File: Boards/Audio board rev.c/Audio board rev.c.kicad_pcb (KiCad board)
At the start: 2 copper layers, 165.9 x 187.4 mm, 110 parts, among them J1 CEC card edge connector large, U1 6821, U10 LM324, U11 MC1458, U2 LM339, U3 LM339, U4 ULN2003A, U5 DAC-08, U6 DAC-08, U7 DAC-08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

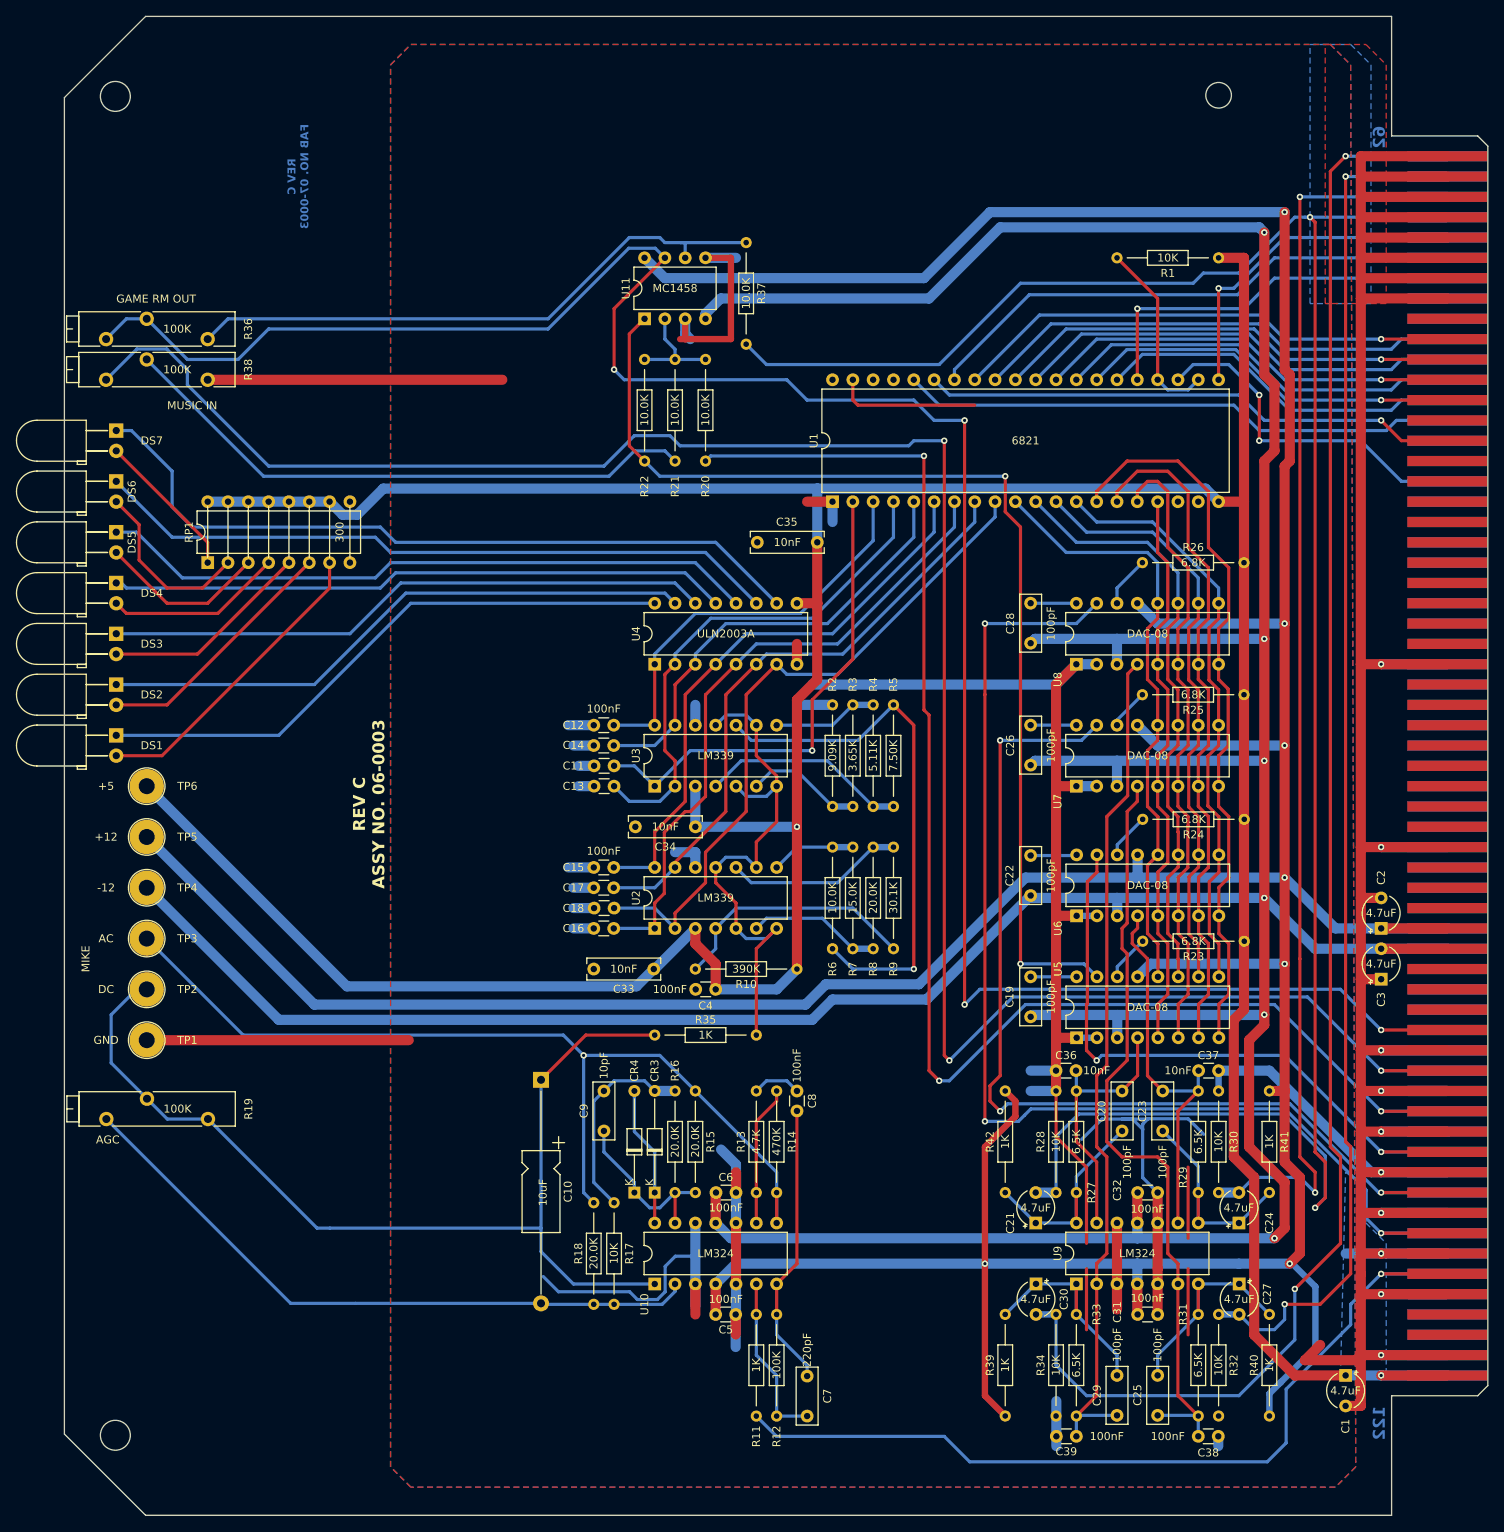
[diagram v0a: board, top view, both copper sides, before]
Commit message: tweaked copper fills on revc
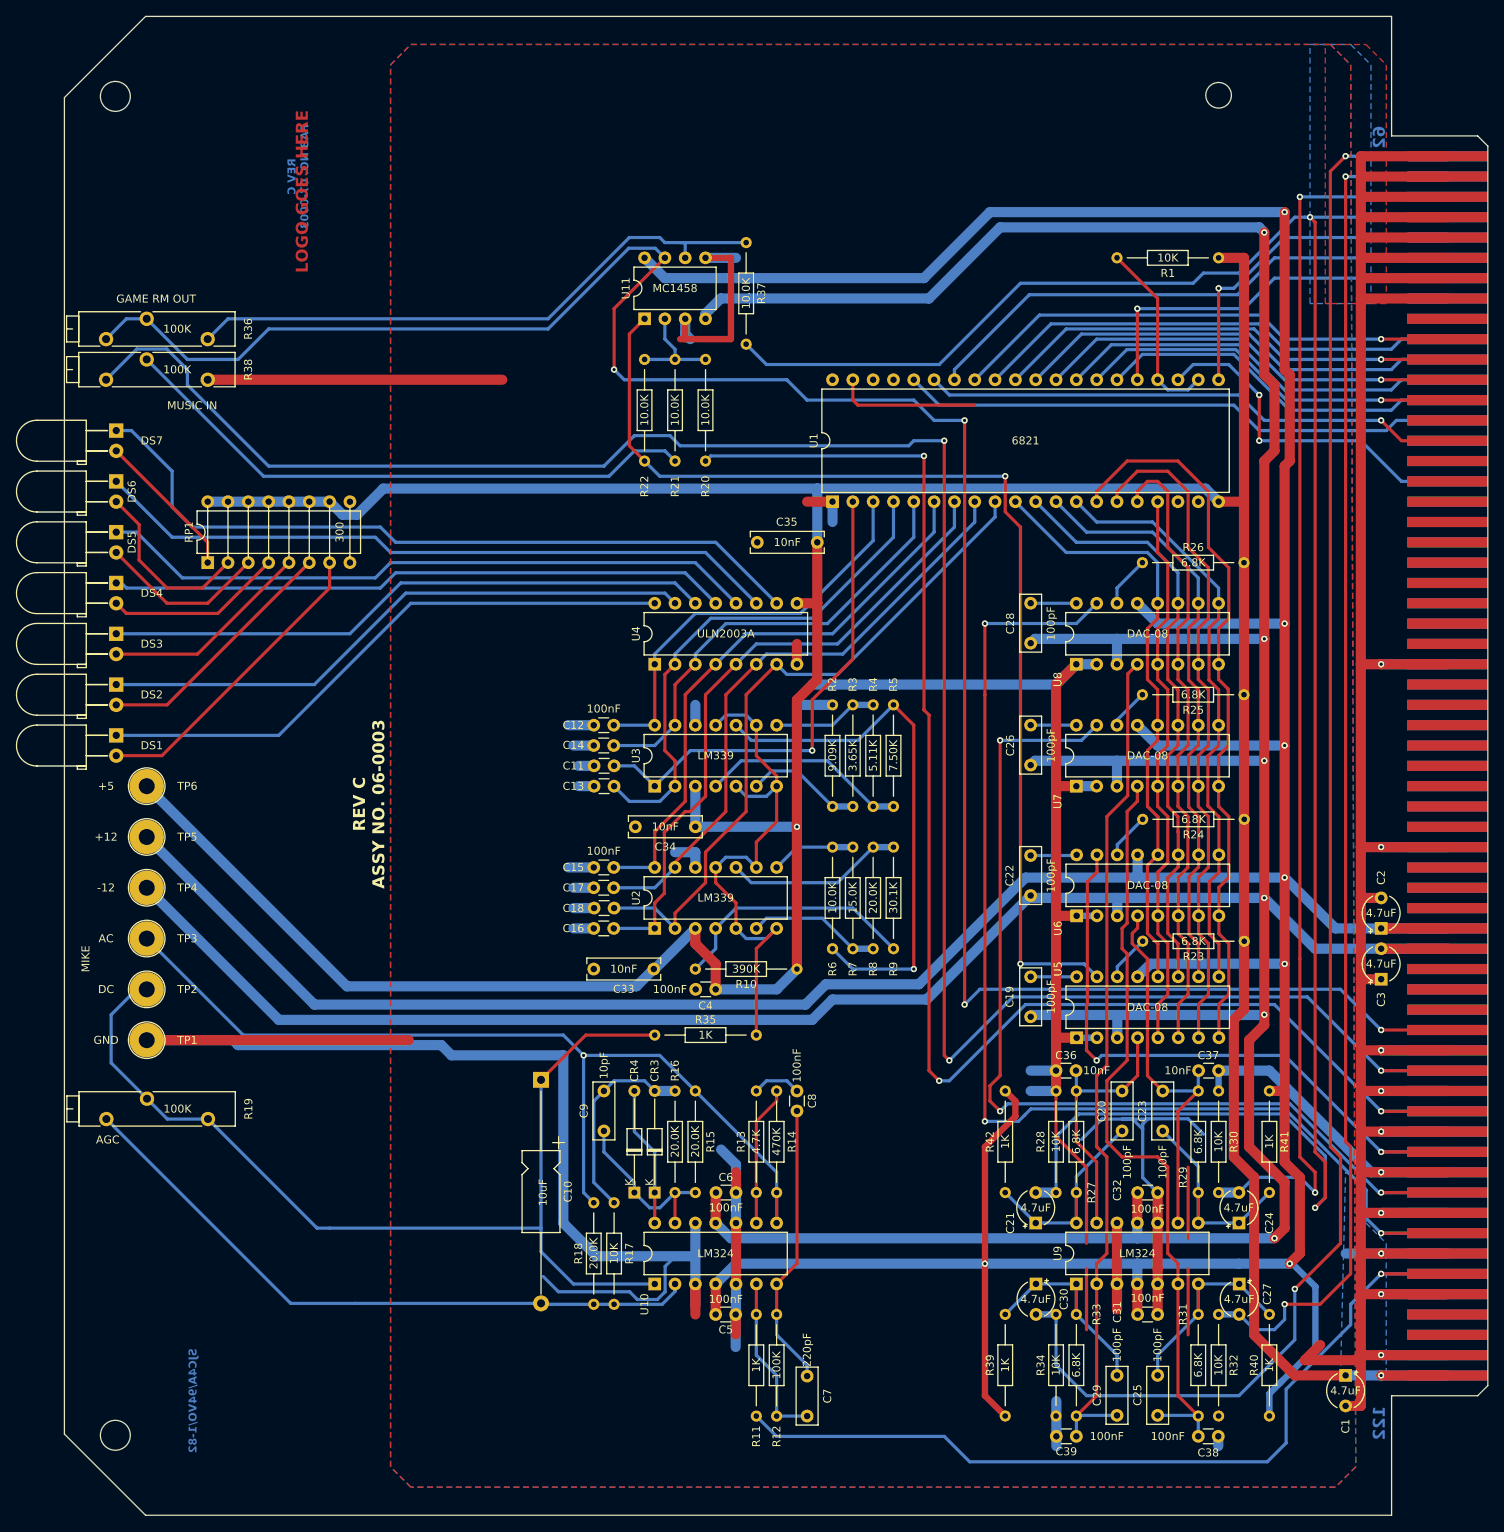
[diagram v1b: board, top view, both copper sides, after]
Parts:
- R27, R29, R31, R33: value 6.5K -> 6.8K
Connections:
- U6 pad 15: unconnected-(U6-Vref--Pad15) -> R2R_audio_track
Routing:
- net GND: track 917.6 -> 1007.8 mm
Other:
- board text added: "LOGO GOES HERE"
- board text added: "SJC4A/94VO/1-82"

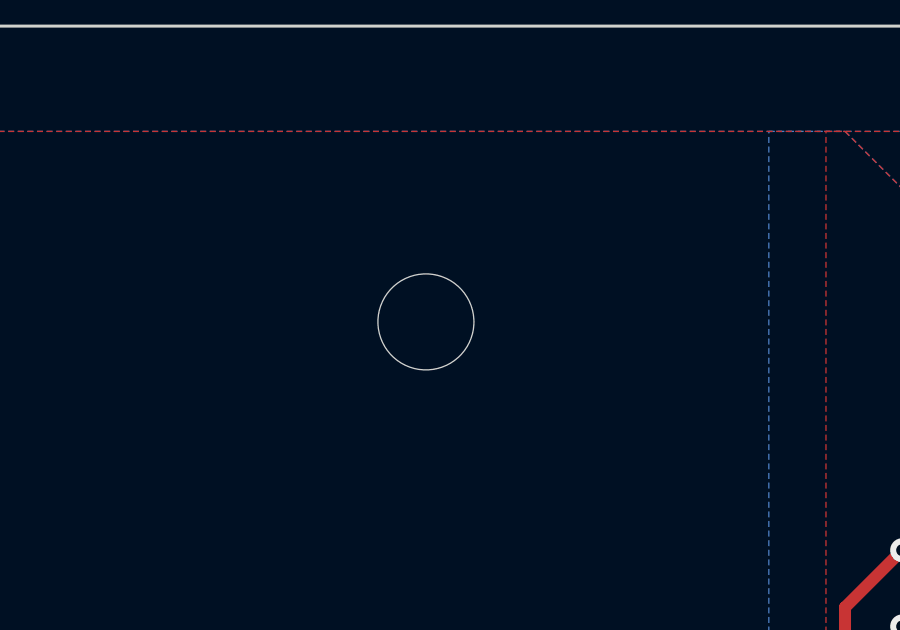
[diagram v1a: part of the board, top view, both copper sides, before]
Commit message: revised hole position in audio cards based on character card
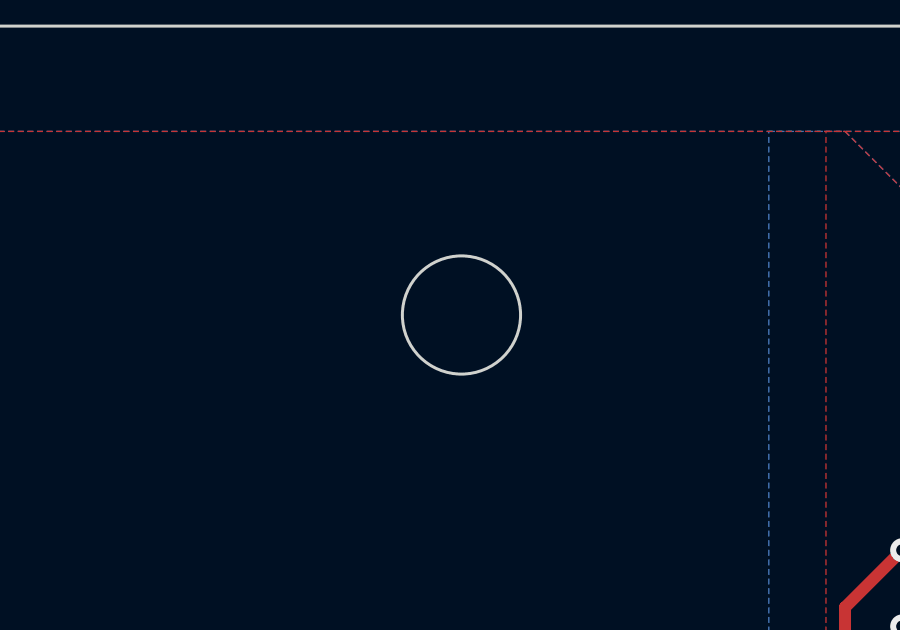
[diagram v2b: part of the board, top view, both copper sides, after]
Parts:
- removed REF**: MountingHole_3.2mm_M3, MountingHole:MountingHole_3.2mm_M3
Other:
- outline, holes or cut-outs redrawn
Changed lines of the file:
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@@
     )
   )
-  (footprint "MountingHole:MountingHole_3.2mm_M3" (layer "F.Cu")
-    (at 201.295 17.155)
-    (descr "Mounting Hole 3.2mm, no annular, M3")
-    (tags "mounting hole 3.2mm no annular m3")
-    (attr exclude_from_pos_files exclude_from_bom)
-    (fp_text reference "REF**" (at 0 -4.2) (layer "F.SilkS") hide
-        (effects (font (size 1 1) (thickness 0.15)))
-    )
-    (fp_text value "MountingHole_3.2mm_M3" (at 0 4.2) (layer "F.Fab")
-        (effects (font (size 1 1) (thickness 0.15)))
-    )
-    (fp_text user "${REFERENCE}" (at 0 0) (layer "F.Fab")
-        (effects (font (size 1 1) (thickness 0.15)))
-    )
-    (fp_circle (center 0 0) (end 3.2 0)
-      (stroke (width 0.15) (type solid)) (fill none) (layer "Cmts.User"))
-    (fp_circle (center 0 0) (end 3.45 0)
-      (stroke (width 0.05) (type solid)) (fill none) (layer "F.CrtYd"))
-    (pad "" np_thru_hole circle (at 0 0) (size 3.2 3.2) (drill 3.2) (layers "*.Cu" "*.Mask"))
-  )
   (footprint "TestPoint:TestPoint_Plated_Hole_D3.0mm" (layer "F.Cu")
     (at 67.31 128.915 180)
@@
   (gr_line (start 222.92 22.235) (end 222.92 7.295)
     (stroke (width 0.1) (type default)) (layer "Edge.Cuts"))
+  (gr_circle (center 202.48 16.925) (end 204.45 16.925)
+    (stroke (width 0.1) (type default)) (fill none) (layer "Edge.Cuts"))
   (gr_circle (center 63.39 184.655) (end 63.39 182.785)
     (stroke (width 0.1) (type default)) (fill none) (layer "Edge.Cuts"))

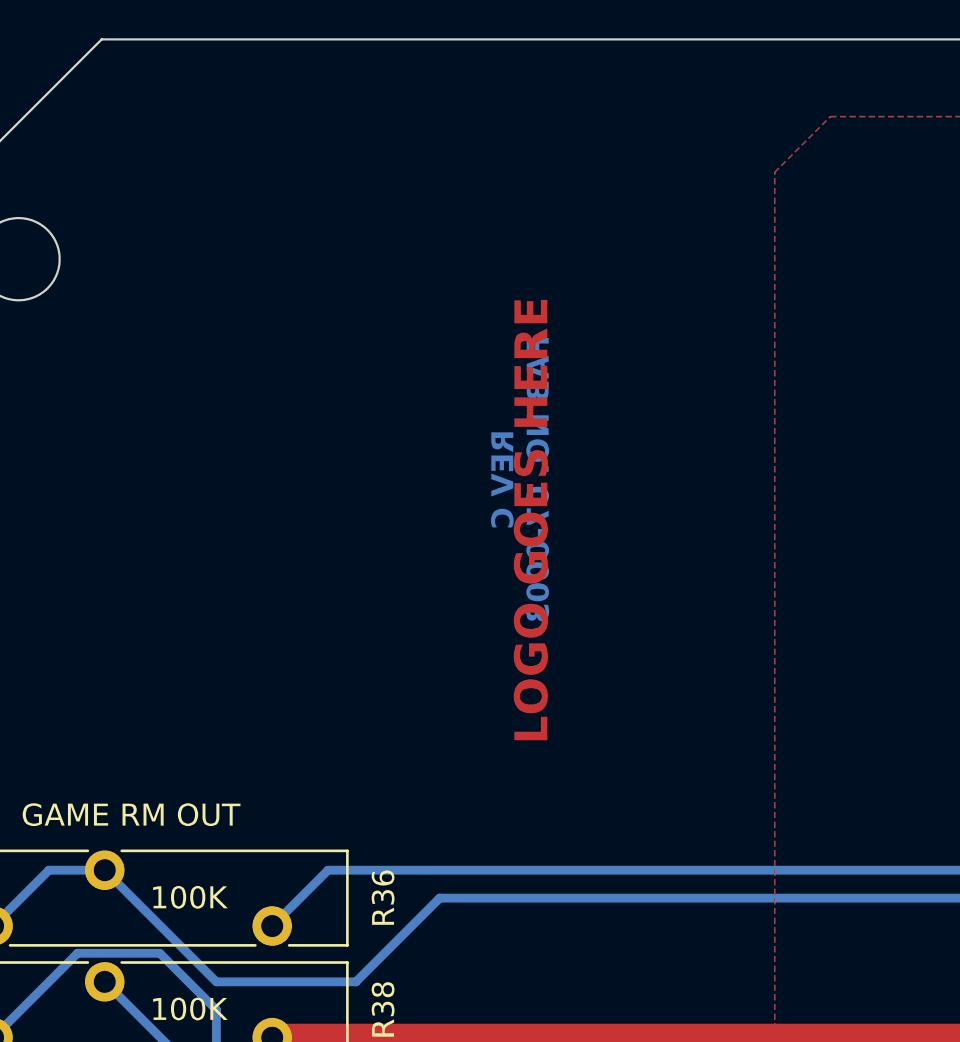
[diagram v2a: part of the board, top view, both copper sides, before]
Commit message: updated boards to have correct logos
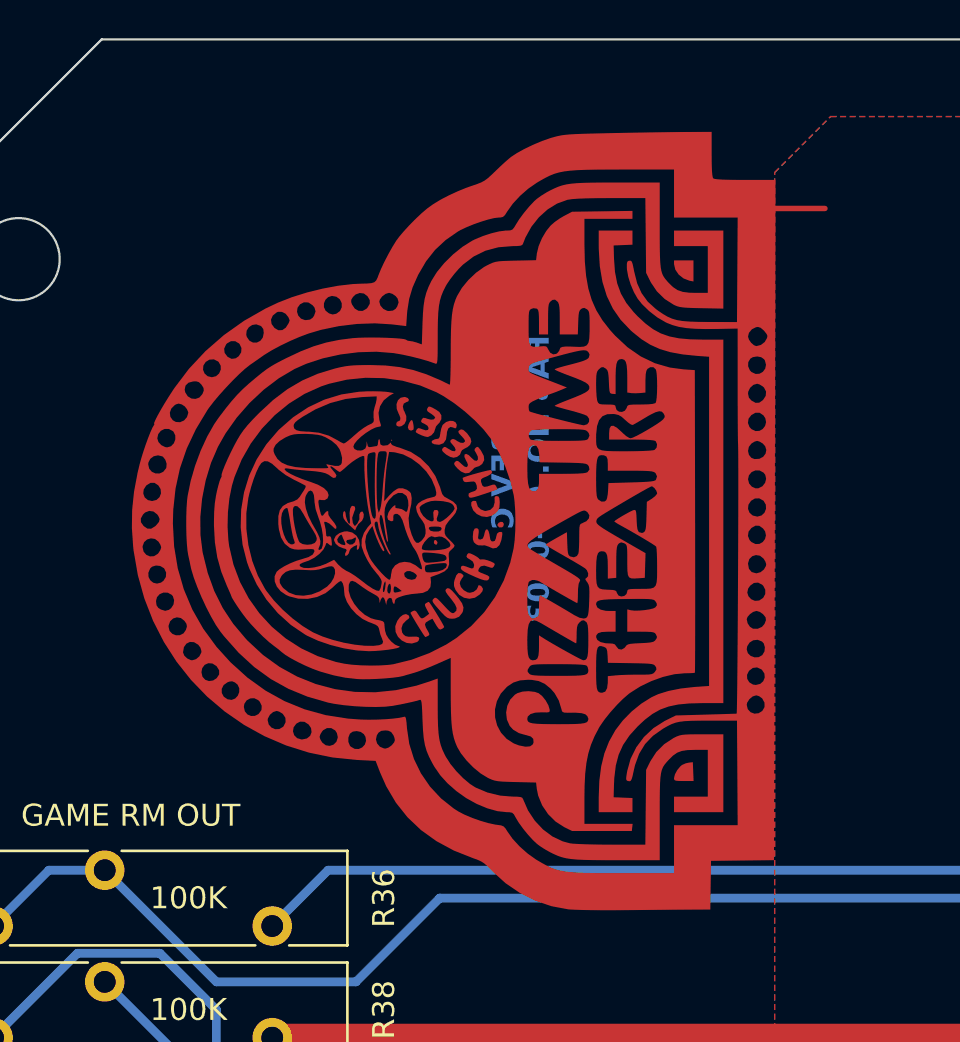
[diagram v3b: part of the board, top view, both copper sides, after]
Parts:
- added G***: LOGO, Evan's parts:PTT black, F.Cu at (83.2, 30.2)
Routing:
- net GND: track 1007.8 -> 1010.7 mm
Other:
- board text removed: "LOGO GOES HERE"
